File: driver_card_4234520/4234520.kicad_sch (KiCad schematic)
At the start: 30 parts, among them J1 Bus_ISA_8bit, J2 DC62_Female, U1 74LS74, U10 74LS155, U11 74LS02, U12 74LS09, U13 74LS244, U14 74LS244, U15 74LS21, U16 74LS244, U17 74LS374, U18 74LS374, U19 74LS374, U2 74LS08, U20 74LS245, U21 74LS244, U22 74LS244, U23 74LS244, U24 74LS32, U3 74LS04, U4 74LS74, U5 74LS32, U6 74LS10, U7 74LS74, U8 74LS138, U9 74LS00

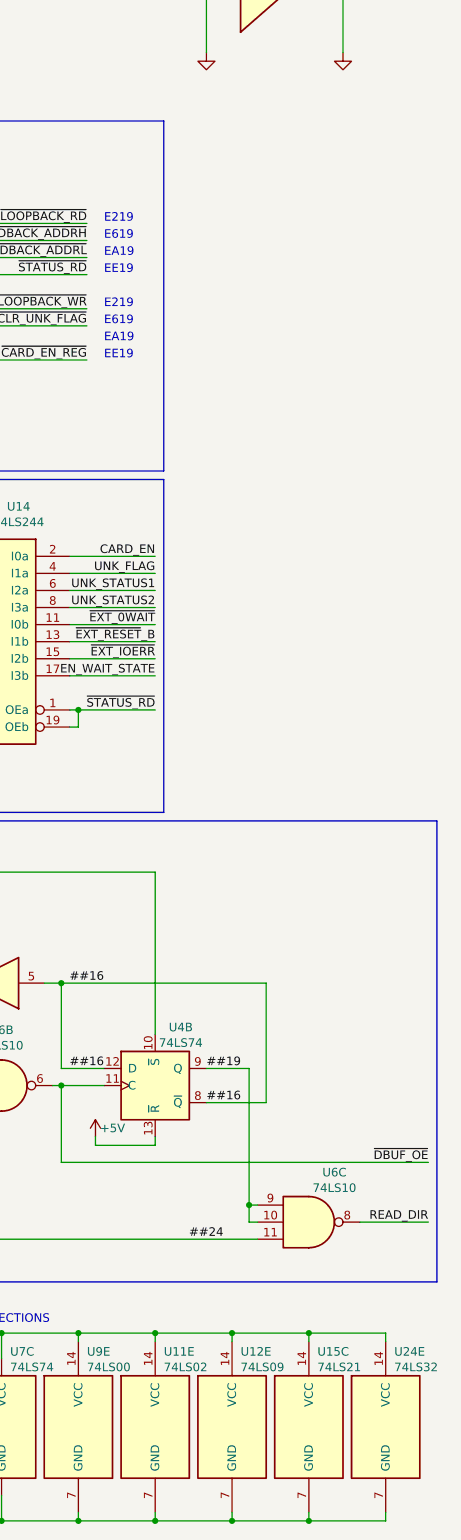
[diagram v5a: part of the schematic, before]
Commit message: add back filter caps
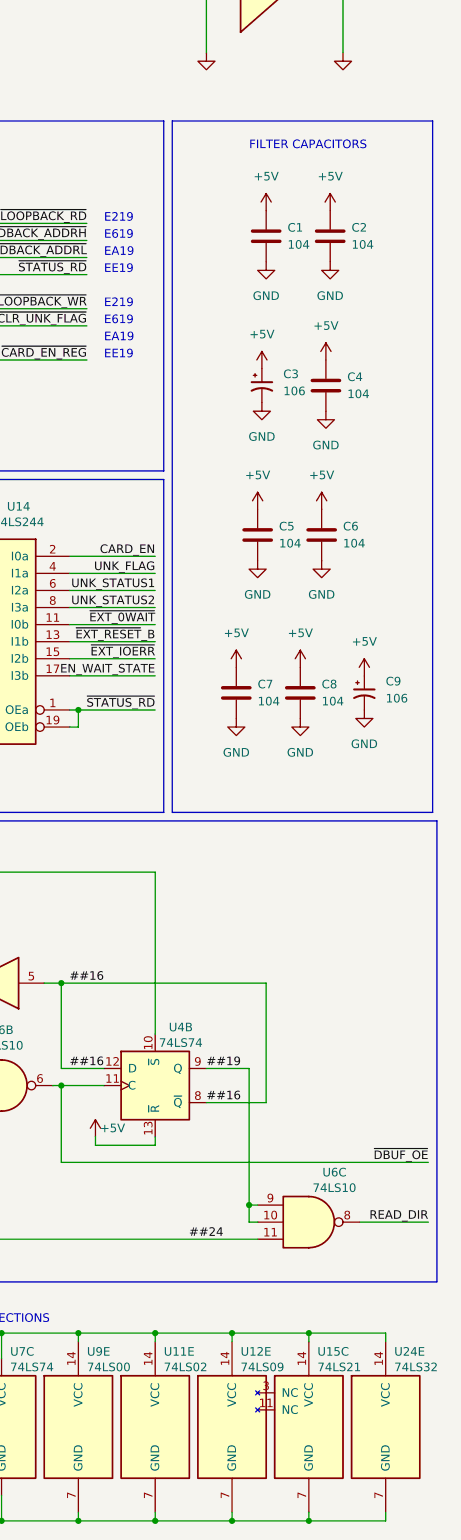
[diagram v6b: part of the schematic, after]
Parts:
- added C1, C2, C4, C5, C6, C7, C8: 104, Capacitor_THT:C_Rect_L7.0mm_W2.0mm_P5.00mm, symbol Device:C
- added C3, C9: 106, Capacitor_THT:C_Rect_L7.0mm_W2.0mm_P5.00mm, symbol Device:C_Polarized_Small_US
- J1: footprint (none) -> custom:BUS_XT
- J2: footprint (none) -> Connector_Dsub:DSUB-62-HD_Female_Horizontal_P2.41x1.98mm_EdgePinOffset3.03mm_Housed_MountingHolesOffset4.94mm
- U1, U11, U12, U15, U2, U24, U3, U4, U5, U6, U7, U9: footprint (none) -> Package_DIP:DIP-14_W7.62mm
- U10, U8: footprint (none) -> Package_DIP:DIP-16_W7.62mm
- U13, U14, U16, U17, U18, U19, U20, U21, U22, U23: footprint (none) -> Package_DIP:DIP-20_W7.62mm
- U15: footprint (none) -> Package_DIP:DIP-14_W7.62mm; symbol 74xx:74LS21 -> custom:74LS21
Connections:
- net +5V: now also C1.1, C2.1, C3.1, C4.1, C5.1, C6.1, C7.1, C8.1, C9.1
- net GND: now also C1.2, C2.2, C3.2, C4.2, C5.2, C6.2, C7.2, C8.2, C9.2
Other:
- note added: "FILTER CAPACITORS"
